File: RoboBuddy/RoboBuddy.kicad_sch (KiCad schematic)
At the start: 26 parts, among them J1 USB_B_Micro, J2 Conn_01x02, U1 RP2040, U2 NCP1117-3.3_SOT223, U3 W25Q128JVS, Y1 ABM8-272-T3

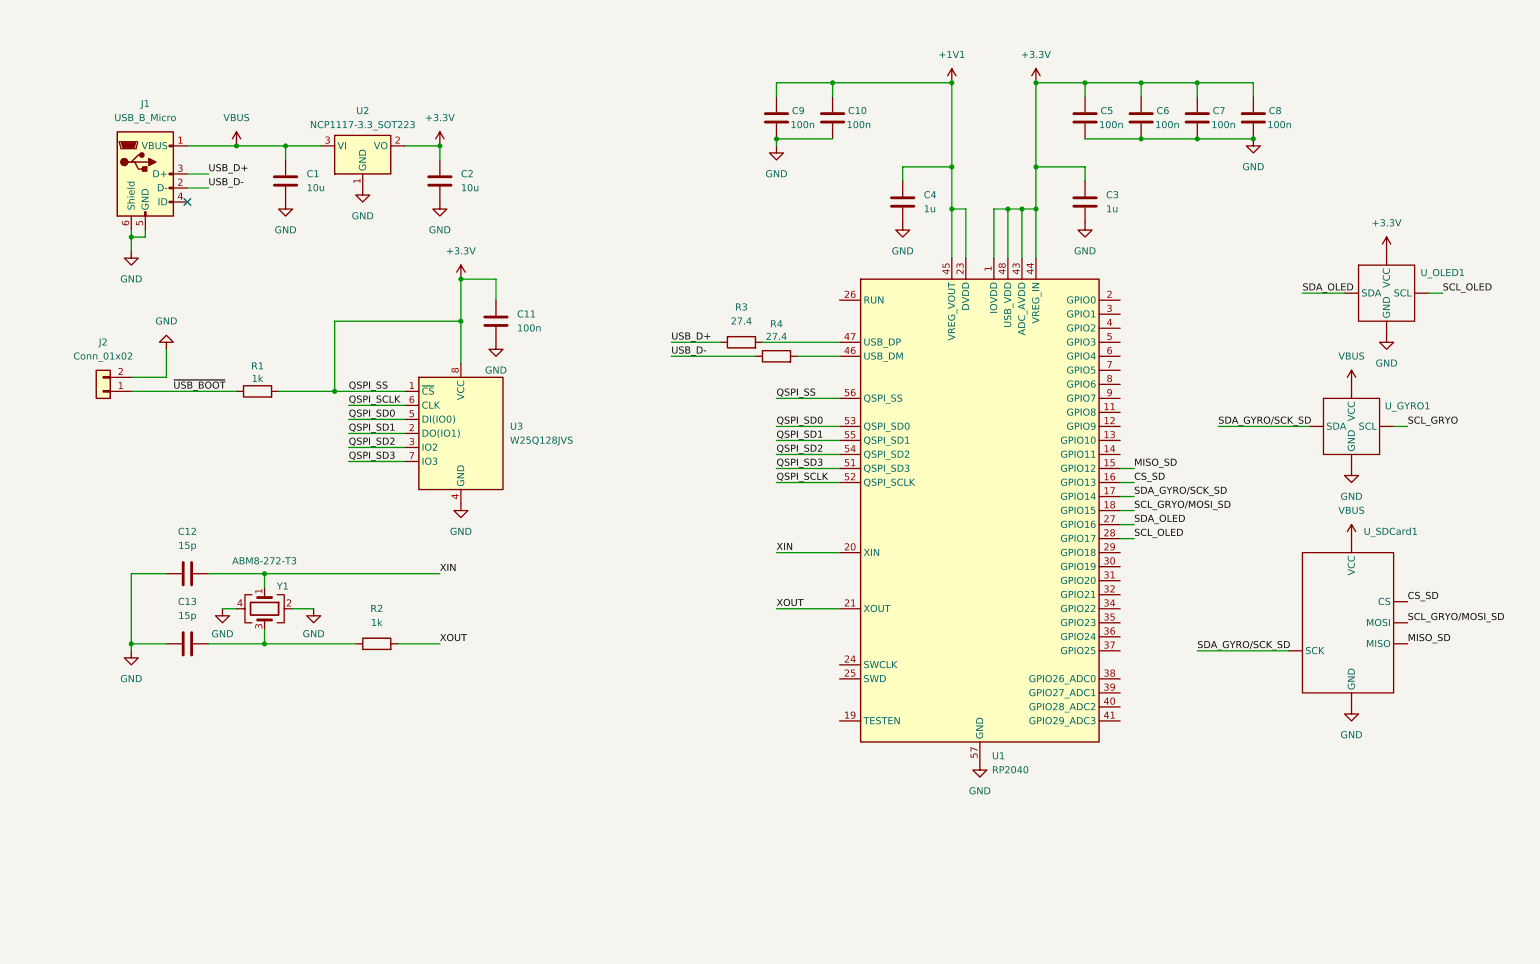
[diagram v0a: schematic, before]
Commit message: Add files via upload
Changes:
- looked at kicad and jlcpcb.com to select some IC to put on my PCB
- added SD card and gyro/accelerometer IC to PCB schematic
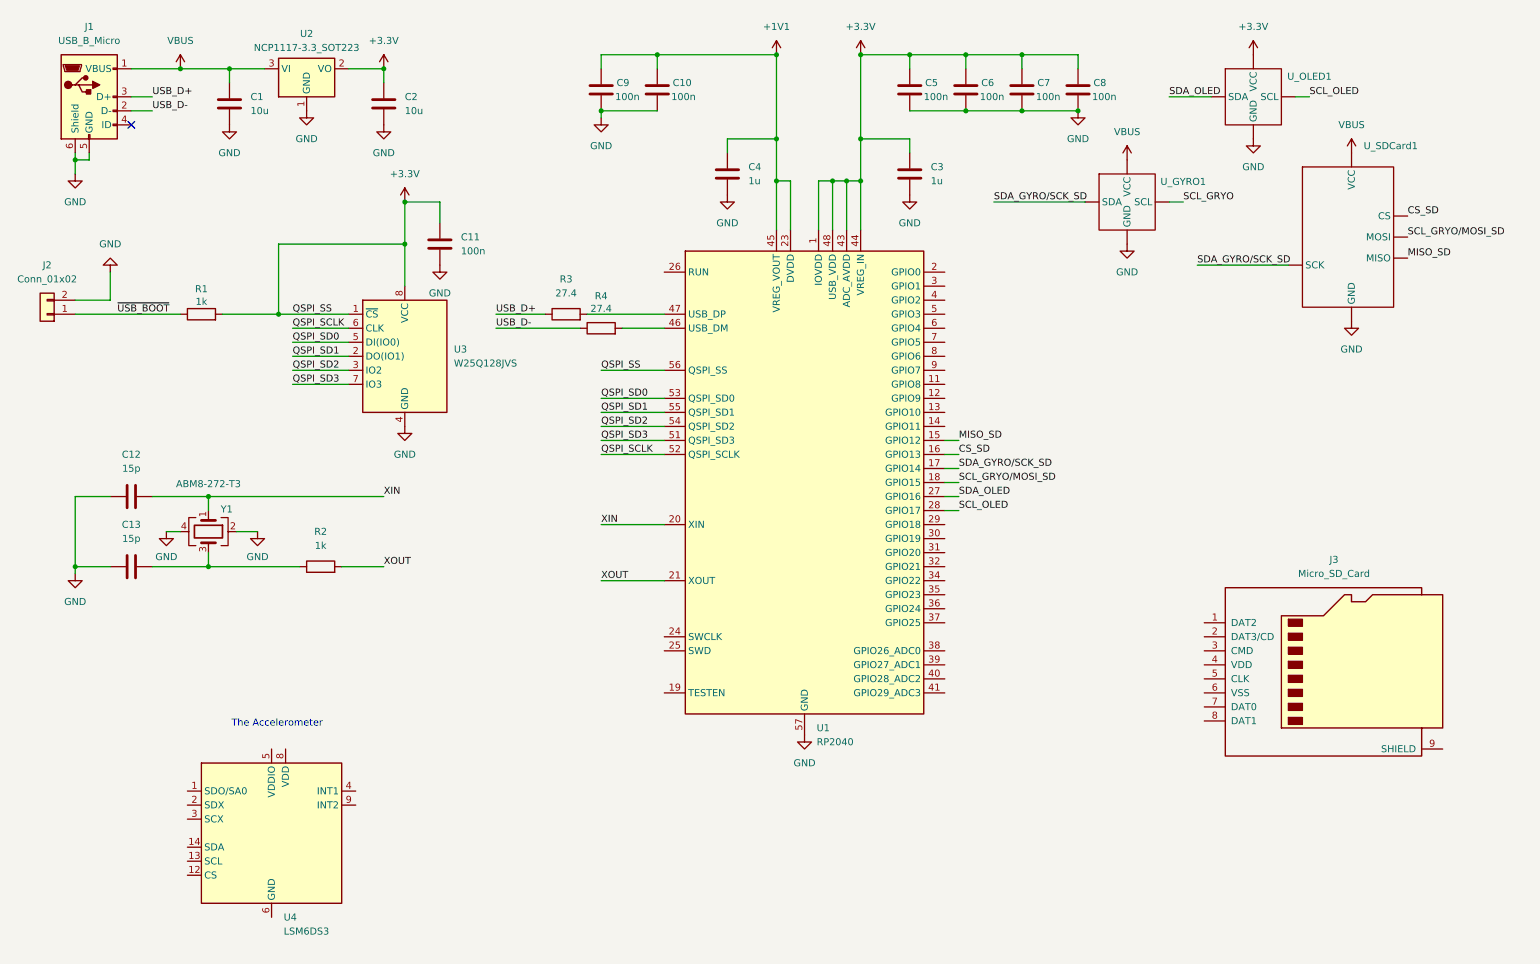
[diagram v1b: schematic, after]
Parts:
- added J3: Micro_SD_Card, Connector_Card:microSD_HC_Molex_104031-0811, symbol Connector:Micro_SD_Card
- added U4: LSM6DS3, Package_LGA:LGA-14_3x2.5mm_P0.5mm_LayoutBorder3x4y, symbol Sensor_Motion:LSM6DS3
- J1: footprint (none) -> Connector_USB:USB_Micro-B_Amphenol_10104110_Horizontal
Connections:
- new net: U4.6 (GND), U4.7 (GND)
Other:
- note added: "The Accelerometer"
- title: (none) -> RoboBuddy
- moved on the sheet: C1, C10, C11, C12, C13, C2, C3, C4, C5, C6, C7, C8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

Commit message: Add files via upload
Roughly added the connections and necessary components for Micro SD card reader and Accelerometer/Gyro modules to the RP2040
- added pullup resistors
- added decoupling capacitors
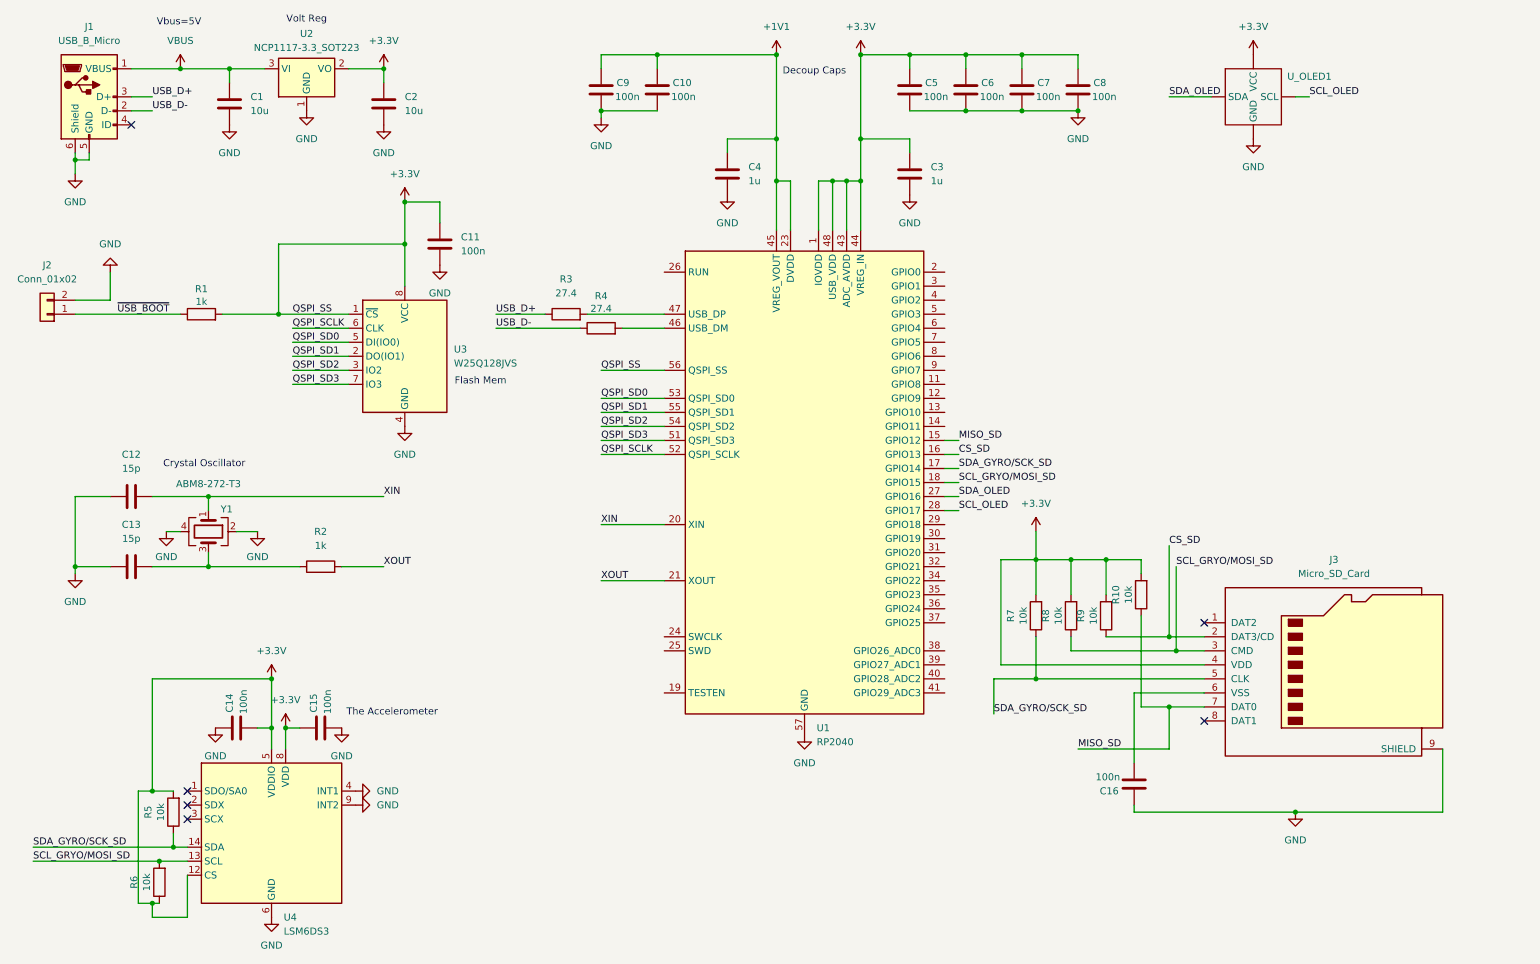
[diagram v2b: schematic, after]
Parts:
- removed U_GYRO1: ~, symbol RoboBuddyLib:Gyro_MPU6050
- removed U_SDCard1: ~, symbol RoboBuddyLib:SDCard_HW125
- added C14, C15, C16: 100n, symbol Device:C
- added R10, R5, R6, R7, R8, R9: 10k, symbol Device:R
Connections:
- net +3.3V: now also J3.4 (VDD), U4.12 (CS), U4.5 (VDDIO), U4.8 (VDD), C14.2, C15.1, R10.2, R5.2, R6.1, R7.2, R8.2, R9.2
- net CS_SD: now also J3.2 (DAT3/CD), R9.1
- net GND: now also J3.9 (SHIELD), U4.4 (INT1), U4.6 (GND), U4.7 (GND), U4.9 (INT2), C14.1, C15.2, C16.1
- net MISO_SD: now also J3.7 (DAT0), R10.1
- net SCL_GRYO/MOSI_SD: now also J3.3 (CMD), U4.13 (SCL), R6.2, R8.1
- net SDA_GYRO/SCK_SD: now also J3.5 (CLK), U4.14 (SDA), R5.1, R7.1
- net at J3.6 (VSS): now also C16.2
- no-connect marks 1 -> 6
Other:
- note added: "Crystal Oscillator"
- note added: "Decoup Caps"
- note added: "Flash Mem"
- note added: "Vbus=5V"
- note added: "Volt Reg"

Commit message: Add files via upload
Finalized the schematic and started on the pcb design
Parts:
- removed J2: Conn_01x02, symbol Connector_Generic:Conn_01x02
- removed U_OLED1: ~, symbol RoboBuddyLib:OLED_SSD1106
- C1, C10, C11, C12, C13, C14, C15, C16, C2, C3, C4, C5, C6, C7, C8, C9: footprint (none) -> Capacitor_SMD:C_0201_0603Metric
- R1, R10, R2, R3, R4, R5, R6, R7, R8, R9: footprint (none) -> Resistor_SMD:R_0201_0603Metric
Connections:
- net GPIO_9: now reaches U1.12 (GPIO9)
- net GPIO_10: now reaches U1.13 (GPIO10)
- net speaker: now reaches U1.14 (GPIO11)
- net TESTEN: now reaches U1.19 (TESTEN)
- net SWCLK: now reaches U1.24 (SWCLK)
- net SWD: now reaches U1.25 (SWD)
- net RUN: now reaches U1.26 (RUN)
- net GPIO_18: now reaches U1.29 (GPIO18)
- net GPIO_19: now reaches U1.30 (GPIO19)
- net GPIO_26_ADC0: now reaches U1.38 (GPIO26_ADC0)
- net ~{USB_BOOT} renamed Pad
- no-connect marks 6 -> 24
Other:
- note added: "VREG_VOUT gives the 1v1 supply"
- note added: "removed the oled placeholder remember to add connections for the 3.3V, GND, and 2 ports SDA and SCL on pins GPIO 16/17"
- moved on the sheet: C16, J3, R10, R7, R8, R9

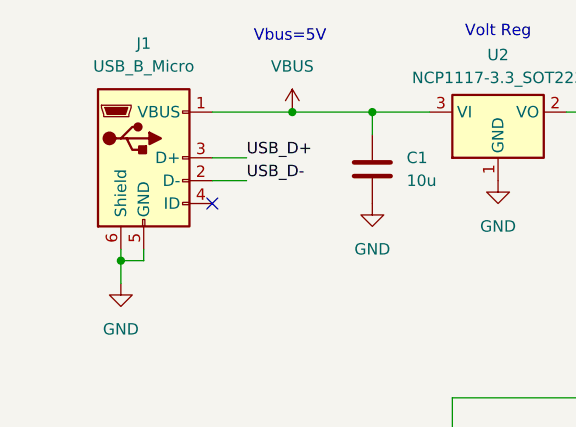
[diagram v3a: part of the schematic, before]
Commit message: Add files via upload
Finished the connecting everything on the pcb schematic. I will now get rid of some of the overlapping silkscreen (mainly getting rid of the capacitors and resistors tags)
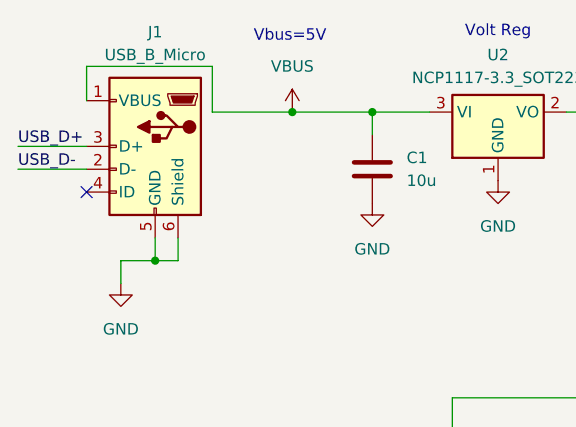
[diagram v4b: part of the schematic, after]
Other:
- moved on the sheet: J1
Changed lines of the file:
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@@
 	)
 	(junction
+		(at 27.94 39.37)
+		(diameter 0)
+		(color 0 0 0 0)
+	)
+	(junction
 		(at 38.1 153.67)
 		(diameter 0)
@@
 	)
 	(junction
-		(at 24.13 39.37)
-		(diameter 0)
-		(color 0 0 0 0)
-	)
-	(junction
 		(at 195.58 20.32)
 		(diameter 0)
@@
 	)
 	(no_connect
-		(at 34.29 33.02)
+		(at 20.32 31.75)
 	)
 	(no_connect
@@
 	(wire
 		(pts
-			(xy 24.13 39.37) (xy 24.13 41.91)
-		)
-		(stroke
-			(width 0)
-			(type default)
-		)
-	)
-	(wire
-		(pts
 			(xy 231.14 125.73) (xy 237.49 125.73)
 		)
@@
 	(wire
 		(pts
-			(xy 166.37 43.18) (xy 163.83 43.18)
+			(xy 24.13 39.37) (xy 27.94 39.37)
 		)
 		(stroke
@@
 	(wire
 		(pts
-			(xy 38.1 173.99) (xy 35.56 173.99)
+			(xy 166.37 43.18) (xy 163.83 43.18)
 		)
 		(stroke
@@
 	(wire
 		(pts
-			(xy 119.38 92.71) (xy 130.81 92.71)
+			(xy 38.1 173.99) (xy 35.56 173.99)
 		)
 		(stroke
@@
 	(wire
 		(pts
-			(xy 213.36 128.27) (xy 213.36 125.73)
+			(xy 119.38 92.71) (xy 130.81 92.71)
 		)
 		(stroke
@@
 	(wire
 		(pts
-			(xy 24.13 39.37) (xy 26.67 39.37)
+			(xy 213.36 128.27) (xy 213.36 125.73)
 		)
 		(stroke
@@
 	(wire
 		(pts
-			(xy 26.67 38.1) (xy 26.67 39.37)
+			(xy 20.32 17.78) (xy 20.32 21.59)
 		)
 		(stroke
@@
 	(wire
 		(pts
-			(xy 34.29 27.94) (xy 38.1 27.94)
-		)
-		(stroke
-			(width 0)
-			(type default)
-		)
-	)
-	(wire
-		(pts
 			(xy 158.75 52.07) (xy 158.75 43.18)
 		)
@@
 	(wire
 		(pts
+			(xy 30.48 36.83) (xy 30.48 39.37)
+		)
+		(stroke
+			(width 0)
+			(type default)
+		)
+	)
+	(wire
+		(pts
 			(xy 64.77 142.24) (xy 62.23 142.24)
 		)
@@
 	(wire
 		(pts
+			(xy 30.48 39.37) (xy 27.94 39.37)
+		)
+		(stroke
+			(width 0)
+			(type default)
+		)
+	)
+	(wire
+		(pts
 			(xy 158.75 43.18) (xy 161.29 43.18)
 		)
@@
 	(wire
 		(pts
+			(xy 24.13 39.37) (xy 24.13 41.91)
+		)
+		(stroke
+			(width 0)
+			(type default)
+		)
+	)
+	(wire
+		(pts
 			(xy 24.13 67.31) (xy 43.18 67.31)
 		)
@@
 	(wire
 		(pts
+			(xy 34.29 22.86) (xy 34.29 17.78)
+		)
+		(stroke
+			(width 0)
+			(type default)
+		)
+	)
+	(wire
+		(pts
 			(xy 199.39 133.35) (xy 207.01 133.35)
 		)
@@
 	(wire
 		(pts
+			(xy 34.29 17.78) (xy 20.32 17.78)
+		)
+		(stroke
+			(width 0)
+			(type default)
+		)
+	)
+	(wire
+		(pts
 			(xy 151.13 43.18) (xy 151.13 52.07)
 		)
@@
 	(wire
 		(pts
-			(xy 34.29 30.48) (xy 38.1 30.48)
+			(xy 60.96 54.61) (xy 83.82 54.61)
 		)
 		(stroke
@@
 	(wire
 		(pts
-			(xy 60.96 54.61) (xy 83.82 54.61)
+			(xy 12.7 29.21) (xy 20.32 29.21)
 		)
 		(stroke
@@
 	(wire
 		(pts
+			(xy 12.7 26.67) (xy 20.32 26.67)
+		)
+		(stroke
+			(width 0)
+			(type default)
+		)
+	)
+	(wire
+		(pts
 			(xy 175.26 20.32) (xy 185.42 20.32)
 		)
@@
 	(wire
 		(pts
-			(xy 24.13 38.1) (xy 24.13 39.37)
+			(xy 27.94 36.83) (xy 27.94 39.37)
 		)
 		(stroke
@@
 	)
 	(label "USB_D-"
-		(at 38.1 30.48 0)
+		(at 12.7 29.21 0)
 		(fields_autoplaced yes)
 		(effects
@@
 	)
 	(label "USB_D+"
-		(at 38.1 27.94 0)
+		(at 12.7 26.67 0)
 		(fields_autoplaced yes)
 		(effects
@@
 	(symbol
 		(lib_id "Connector:USB_B_Micro")
-		(at 26.67 27.94 0)
+		(at 27.94 26.67 0)
+		(mirror y)
 		(unit 1)
 		(exclude_from_sim no)
@@
 		(on_board yes)
 		(dnp no)
-		(fields_autoplaced yes)
 		(property "Reference" "J1"
-			(at 26.67 15.24 0)
+			(at 27.94 13.97 0)
 			(effects
 				(font
@@
 		)
 		(property "Value" "USB_B_Micro"
-			(at 26.67 17.78 0)
+			(at 27.94 16.51 0)
 			(effects
 				(font
@@
 		)
 		(property "Footprint" "Connector_USB:USB_Micro-B_Amphenol_10104110_Horizontal"
-			(at 30.48 29.21 0)
+			(at 24.13 27.94 0)
 			(effects
 				(font
@@
 		)
 		(property "Datasheet" "~"
-			(at 30.48 29.21 0)
+			(at 24.13 27.94 0)
 			(effects
 				(font
@@
 		)
 		(property "Description" "USB Micro Type B connector"
-			(at 26.67 27.94 0)
+			(at 27.94 26.67 0)
 			(effects
 				(font
